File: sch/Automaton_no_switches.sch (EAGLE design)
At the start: 24 parts, among them IC1 74LS595D, IC2 74LS595D, IC3 74LS595D, IC4 74LS595D, J1 POWER_JACKPTH

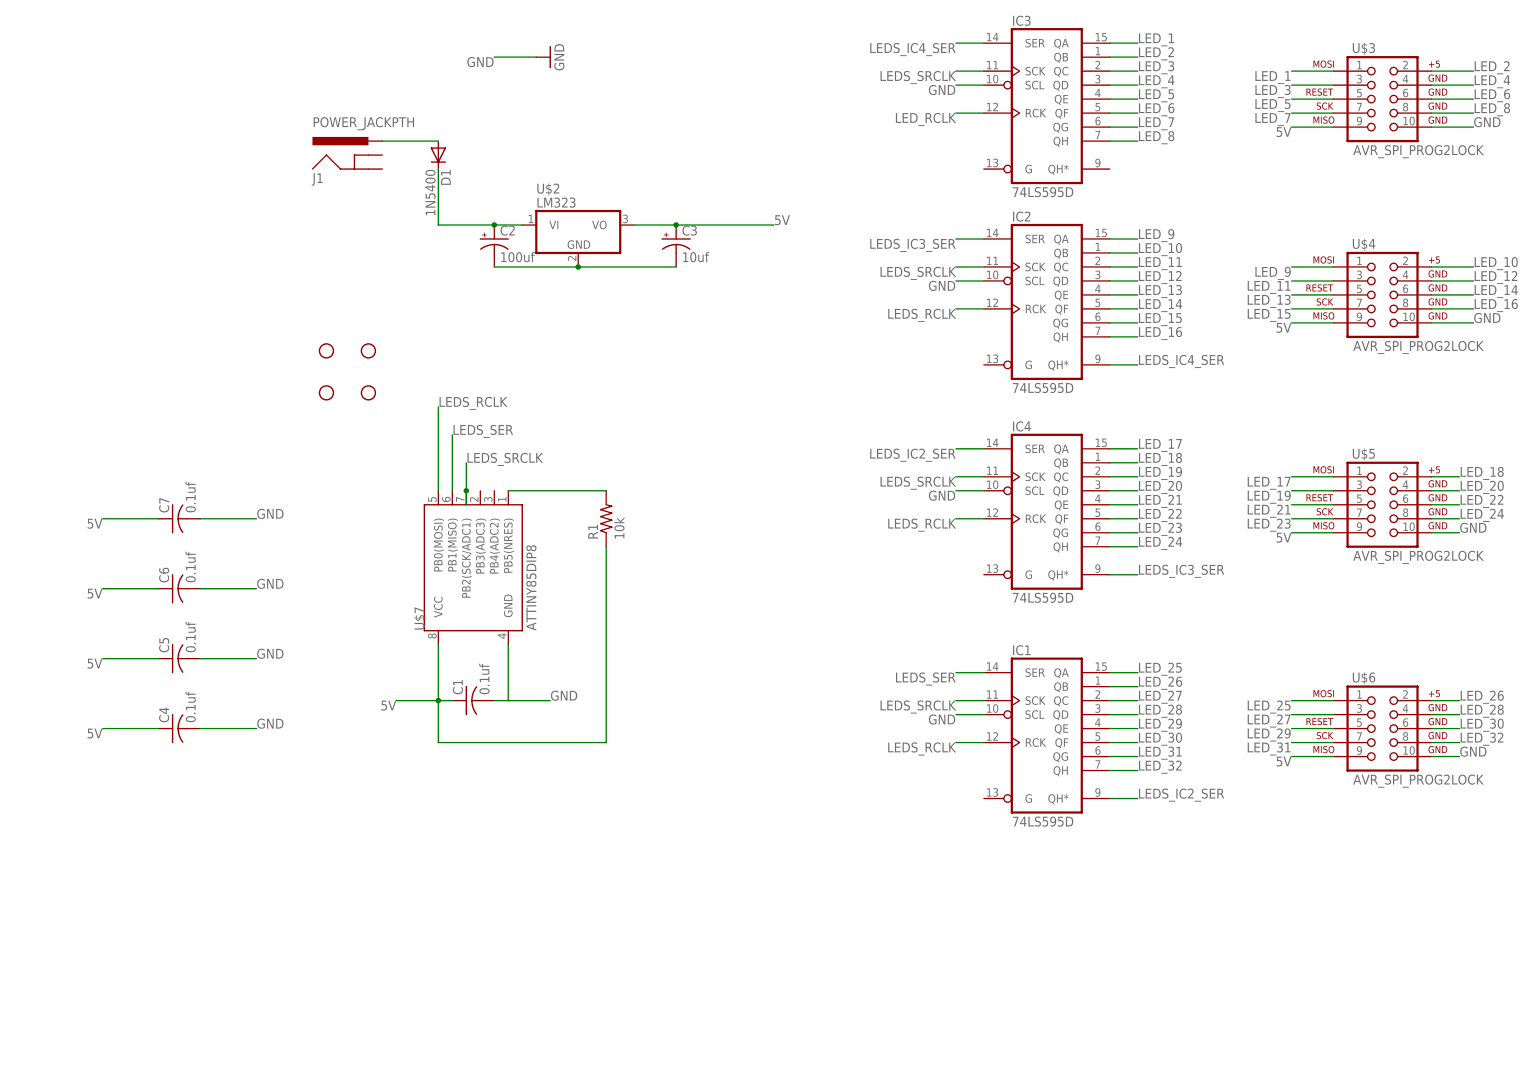
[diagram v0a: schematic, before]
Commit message: added to schematic
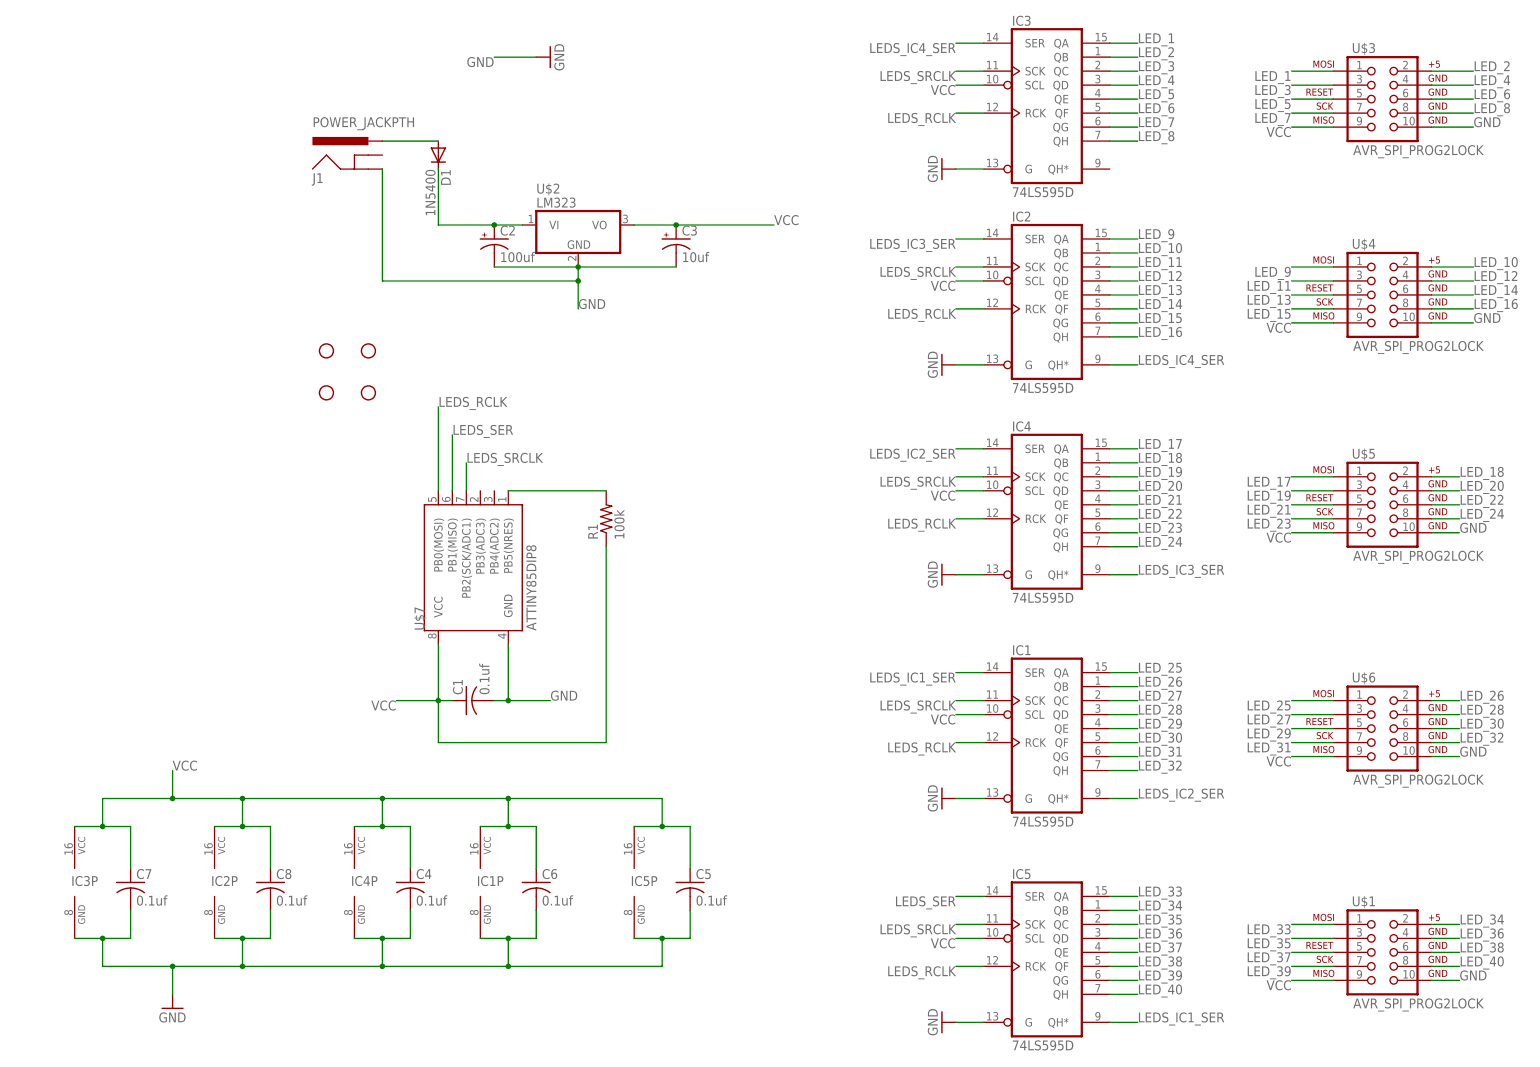
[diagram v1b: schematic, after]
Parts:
- added C8: 0.1uf, resistor:C-USC1206
- added IC5: 74LS595D, 74xx-us:74LS595D
- added U$1: AVR_SPI_PROG2LOCK, SparkFun:AVR_SPI_PROG2LOCK
- C1, C4, C5, C6, C7: device resistor:C-US025-024X044 -> resistor:C-USC1206
- R1: value 10k -> 100k
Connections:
- removed net 5V: C1.1, C3.+, C4.1, C5.1, C6.1, C7.1, R1.1, U$2.VO, U$3.9, U$4.9, U$5.9, U$6.9, U$7.VCC
- removed net LED_RCLK: IC3A.RCK
- removed net N$4: C2.-, C3.-, U$2.GND
- new net LEDS_IC1_SER: IC1A.SER, IC5A.QH*
- new net LED_33: IC5A.QA, U$1.1
- new net LED_34: IC5A.QB, U$1.2
- new net LED_35: IC5A.QC, U$1.3
- new net LED_36: IC5A.QD, U$1.4
- new net LED_37: IC5A.QE, U$1.5
- new net LED_38: IC5A.QF, U$1.6
- new net LED_39: IC5A.QG, U$1.7
- new net LED_40: IC5A.QH, U$1.8
- new net VCC: C1.1, C3.+, C4.1, C5.1, C6.1, C7.1, C8.1, IC1A.SCL, IC1P.VCC, IC2A.SCL, IC2P.VCC, IC3A.SCL, IC3P.VCC, IC4A.SCL, IC4P.VCC, IC5A.SCL, IC5P.VCC, R1.1, U$1.9, U$2.VO, U$3.9, U$4.9, U$5.9, U$6.9, U$7.VCC
- net GND: now also C2.-, C3.-, C8.2, IC1A.G, IC1P.GND, IC2A.G, IC2P.GND, IC3A.G, IC3P.GND, IC4A.G, IC4P.GND, IC5A.G, IC5P.GND, J1.GND, U$1.10, U$2.GND; no longer IC1A.SCL, IC2A.SCL, IC3A.SCL, IC4A.SCL
- net LEDS_RCLK: now also IC3A.RCK, IC5A.RCK
- net LEDS_SER: now also IC5A.SER; no longer IC1A.SER
- net LEDS_SRCLK: now also IC5A.SCK
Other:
- moved on the sheet: C4, C5, C6, C7

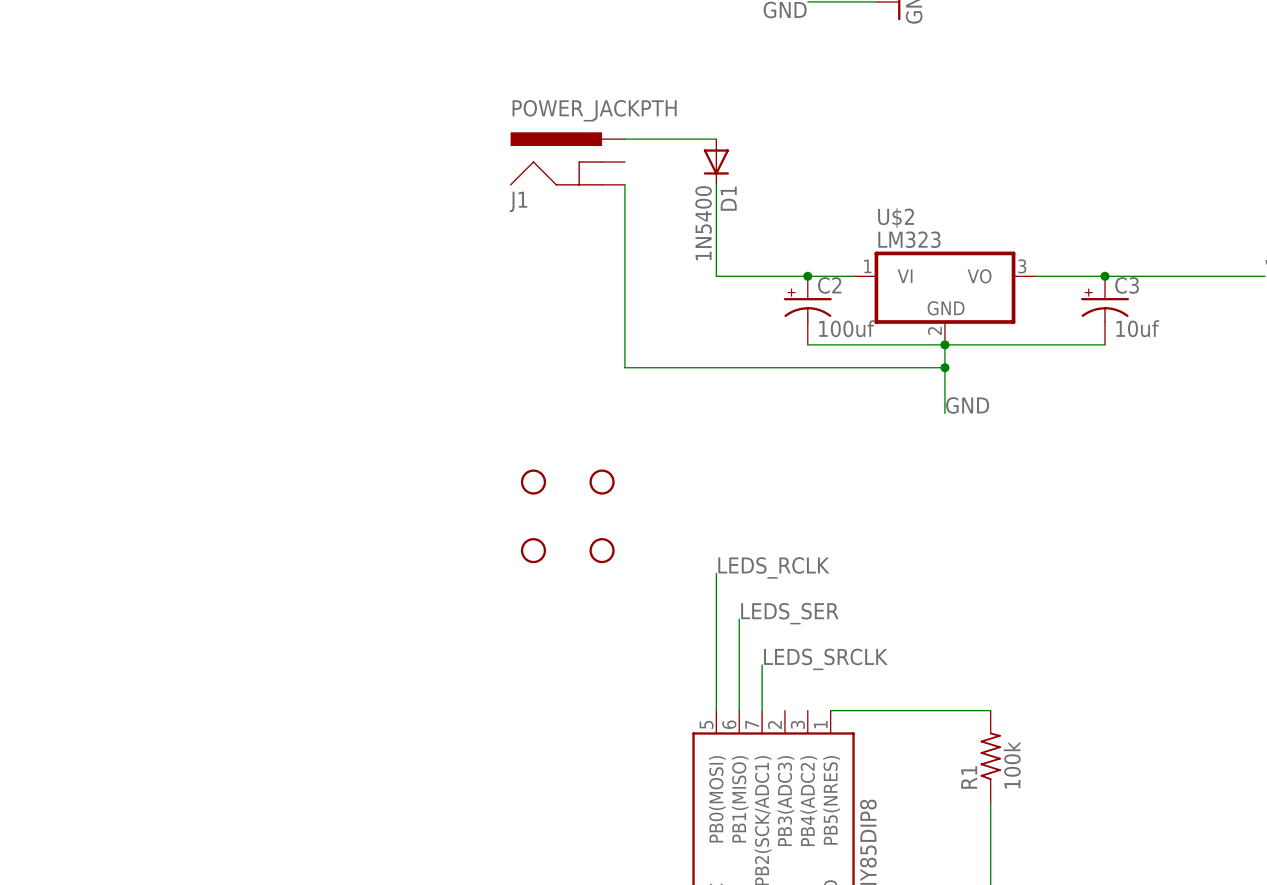
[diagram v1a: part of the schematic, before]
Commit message: board passes batchpcb's DRC now
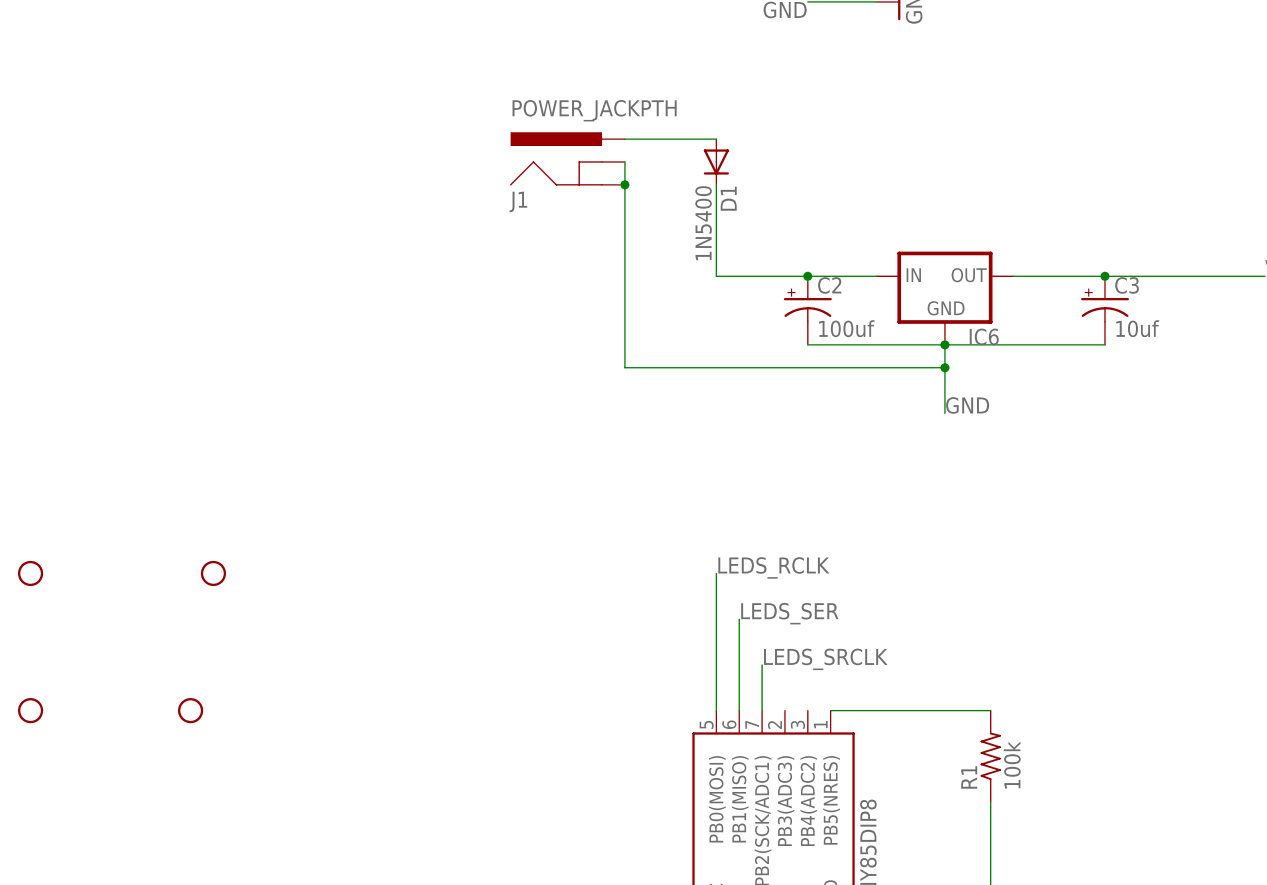
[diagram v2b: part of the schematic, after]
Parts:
- removed U$2: LM323, MyLib:LM323
- added IC6: (no value), SparkFun-PowerIC:V_REG_78XXSINK
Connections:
- net GND: now also IC6.GND, J1.GNDBREAK; no longer U$2.GND
- net N$1: now also IC6.IN; no longer U$2.VI
- net VCC: now also IC6.OUT; no longer U$2.VO
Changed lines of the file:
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@@
 <part name="GND1" library="supply1" deviceset="GND" device=""/>
 <part name="C1" library="resistor" deviceset="C-US" device="C1206" value="0.1uf"/>
-<part name="U$2" library="MyLib" deviceset="LM323" device=""/>
 <part name="U$3" library="SparkFun" deviceset="AVR_SPI_PROG2" device="LOCK"/>
 <part name="U$4" library="SparkFun" deviceset="AVR_SPI_PROG2" device="LOCK"/>
@@
 <part name="C6" library="resistor" deviceset="C-US" device="C1206" value="0.1uf"/>
 <part name="C7" library="resistor" deviceset="C-US" device="C1206" value="0.1uf"/>
-<part name="JP1" library="SparkFun-Electromechanical" deviceset="STAND-OFF" device=""/>
-<part name="JP2" library="SparkFun-Electromechanical" deviceset="STAND-OFF" device=""/>
-<part name="JP3" library="SparkFun-Electromechanical" deviceset="STAND-OFF" device=""/>
-<part name="JP4" library="SparkFun-Electromechanical" deviceset="STAND-OFF" device=""/>
 <part name="R1" library="resistor" deviceset="R-US_" device="M1206" value="100k"/>
 <part name="IC5" library="74xx-us" deviceset="74*595" device="D" technology="LS"/>
@@
 <part name="GND6" library="supply1" deviceset="GND" device=""/>
 <part name="GND7" library="supply1" deviceset="GND" device=""/>
+<part name="IC6" library="SparkFun-PowerIC" deviceset="V_REG_78XX" device="SINK"/>
+<part name="JP1" library="SparkFun-Electromechanical" deviceset="STAND-OFF" device=""/>
+<part name="JP2" library="SparkFun-Electromechanical" deviceset="STAND-OFF" device=""/>
+<part name="JP3" library="SparkFun-Electromechanical" deviceset="STAND-OFF" device=""/>
+<part name="JP4" library="SparkFun-Electromechanical" deviceset="STAND-OFF" device=""/>
 </parts>
 <sheets>
@@
 <instance part="GND1" gate="1" x="53.34" y="7.62" rot="R90"/>
 <instance part="C1" gate="G$1" x="38.1" y="-109.22" rot="R90"/>
-<instance part="U$2" gate="G$1" x="58.42" y="-22.86"/>
 <instance part="U$3" gate="A" x="203.2" y="0"/>
 <instance part="U$4" gate="A" x="203.2" y="-35.56"/>
@@
 <instance part="C6" gate="G$1" x="50.8" y="-142.24"/>
 <instance part="C7" gate="G$1" x="-22.86" y="-142.24"/>
-<instance part="JP1" gate="G$1" x="12.7" y="-53.34"/>
-<instance part="JP2" gate="G$1" x="12.7" y="-45.72"/>
-<instance part="JP3" gate="G$1" x="20.32" y="-45.72"/>
-<instance part="JP4" gate="G$1" x="20.32" y="-53.34"/>
 <instance part="R1" gate="G$1" x="63.5" y="-76.2" rot="R90"/>
 <instance part="IC5" gate="A" x="142.24" y="-154.94"/>
@@
 <instance part="GND6" gate="1" x="124.46" y="-48.26" rot="R270"/>
 <instance part="GND7" gate="1" x="124.46" y="-12.7" rot="R270"/>
+<instance part="IC6" gate="G$1" x="58.42" y="-22.86"/>
+<instance part="JP1" gate="G$1" x="-43.18" y="-55.88"/>
+<instance part="JP2" gate="G$1" x="-22.86" y="-55.88"/>
+<instance part="JP3" gate="G$1" x="-43.18" y="-71.12"/>
+<instance part="JP4" gate="G$1" x="-25.4" y="-71.12"/>
 </instances>
 <busses>
@@
 <wire x1="76.2" y1="-30.48" x2="58.42" y2="-30.48" width="0.2032" layer="91"/>
 <junction x="58.42" y="-30.48"/>
-<pinref part="U$2" gate="G$1" pin="GND"/>
 <pinref part="C2" gate="G$1" pin="-"/>
 <pinref part="C3" gate="G$1" pin="-"/>
@@
 <label x="58.42" y="-38.1" size="1.778" layer="95"/>
 <junction x="58.42" y="-33.02"/>
+<pinref part="J1" gate="G$1" pin="GNDBREAK"/>
+<wire x1="22.86" y1="-10.16" x2="22.86" y2="-12.7" width="0.1524" layer="91"/>
+<junction x="22.86" y="-12.7"/>
+<pinref part="IC6" gate="G$1" pin="GND"/>
 </segment>
 <segment>
@@
 <net name="VCC" class="0">
 <segment>
-<wire x1="68.58" y1="-22.86" x2="76.2" y2="-22.86" width="0.2032" layer="91"/>
 <wire x1="76.2" y1="-22.86" x2="93.98" y2="-22.86" width="0.2032" layer="91"/>
 <label x="93.98" y="-22.86" size="1.778" layer="95"/>
-<pinref part="U$2" gate="G$1" pin="VO"/>
 <pinref part="C3" gate="G$1" pin="+"/>
+<pinref part="IC6" gate="G$1" pin="OUT"/>
+<wire x1="76.2" y1="-22.86" x2="66.04" y2="-22.86" width="0.1524" layer="91"/>
 <junction x="76.2" y="-22.86"/>
 </segment>
@@
 <segment>
 <wire x1="33.02" y1="-22.86" x2="43.18" y2="-22.86" width="0.2032" layer="91"/>
-<pinref part="U$2" gate="G$1" pin="VI"/>
 <pinref part="D1" gate="1" pin="C"/>
-<wire x1="43.18" y1="-22.86" x2="48.26" y2="-22.86" width="0.2032" layer="91"/>
 <wire x1="33.02" y1="-12.7" x2="33.02" y2="-22.86" width="0.1524" layer="91"/>
 <pinref part="C2" gate="G$1" pin="+"/>
+<pinref part="IC6" gate="G$1" pin="IN"/>
+<wire x1="43.18" y1="-22.86" x2="50.8" y2="-22.86" width="0.1524" layer="91"/>
 <junction x="43.18" y="-22.86"/>
 </segment>
